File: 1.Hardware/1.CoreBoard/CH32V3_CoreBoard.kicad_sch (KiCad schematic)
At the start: 53 parts, among them J2 SH1.0_4P, J3 USB-Type-C, J4 BTB_02X18, J5 BTB_02X18, SW1 3x4, SW2 3x4, SW3 3x4, SW4 3x4, U2 RT9013-33GB, U3 BMI270, U5 IPS096, Y1 32.768KHz, Y2 8MHz

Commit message: coreboard
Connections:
- net ENC_2DIR: now also J5.32 (Pin_32); no longer J5.30 (Pin_30)
- net PB12: now also J5.27 (Pin_27); no longer J5.31 (Pin_31)
- net PB14: now also J5.36 (Pin_36); no longer J5.32 (Pin_32)
- net PD10: now also J5.30 (Pin_30); no longer J5.27 (Pin_27)
- net PD8: now also J5.34 (Pin_34); no longer J5.29 (Pin_29)
- net PE14: now also J5.31 (Pin_31); no longer J5.35 (Pin_35)
- net PE15: now also J5.29 (Pin_29); no longer J5.36 (Pin_36)
- net UART7_RX: now also J5.33 (Pin_33); no longer J5.34 (Pin_34)
- net UART7_TX: now also J5.35 (Pin_35); no longer J5.33 (Pin_33)

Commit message: CoreBoard finished
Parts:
- added C22: 100nF, ErBW_s:C_0402, symbol Device:C_Small
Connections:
- net +3.3V: now also C22.2
- net ADC_DIS: now also J4.4 (Pin_4); no longer J4.9 (Pin_9)
- net ADC_VBAT: now also J4.2 (Pin_2); no longer J4.10 (Pin_10)
- net AUX_SCL: now also J4.13 (Pin_13); no longer J4.1 (Pin_1)
- net AUX_SDA: now also J4.11 (Pin_11); no longer J4.2 (Pin_2)
- net BUZZER: now also J4.9 (Pin_9); no longer J4.3 (Pin_3)
- net ENCODER_B: now also U1.3 (PE4); no longer U1.2 (PE3)
- net ENC_1DIR: now also J4.27 (Pin_27); no longer J4.29 (Pin_29)
- net ENC_1LSB: now also J4.23 (Pin_23); no longer J4.27 (Pin_27)
- net GND: now also C22.1
- net KEY_CENTER: now also U1.2 (PE3); no longer U1.3 (PE4)
- net PA0: now also J4.6 (Pin_6); no longer J4.8 (Pin_8)
- net PA15: now also J4.29 (Pin_29); no longer J4.28 (Pin_28)
- net PA3: now also J4.8 (Pin_8); no longer J4.11 (Pin_11)
- net PA7: now also J4.10 (Pin_10); no longer J4.12 (Pin_12)
- net PB0: now also J4.16 (Pin_16); no longer J4.15 (Pin_15)
- net PB1: now also J4.18 (Pin_18); no longer J4.16 (Pin_16)
- net PC0: now also J4.7 (Pin_7); no longer J4.4 (Pin_4)
- net PC2: now also J4.3 (Pin_3); no longer J4.6 (Pin_6)
- net PC3: now also J4.1 (Pin_1); no longer J4.7 (Pin_7)
- net PC4: now also J4.12 (Pin_12); no longer J4.13 (Pin_13)
- net PD2: now also J4.25 (Pin_25); no longer J4.26 (Pin_26)
- net PD5: now also J4.21 (Pin_21); no longer J4.24 (Pin_24)
- net PD6: now also J4.19 (Pin_19); no longer J4.25 (Pin_25)
- net PE0: now also J4.17 (Pin_17); no longer J4.22 (Pin_22)
- net PE1: now also J4.15 (Pin_15); no longer J4.23 (Pin_23)
- net PE10: now also J4.26 (Pin_26); no longer J4.20 (Pin_20)
- net PE11: now also J4.28 (Pin_28); no longer J4.21 (Pin_21)
- net PE7: now also J4.20 (Pin_20); no longer J4.17 (Pin_17)
- net PE8: now also J4.22 (Pin_22); no longer J4.18 (Pin_18)
- net PE9: now also J4.24 (Pin_24); no longer J4.19 (Pin_19)
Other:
- moved on the sheet: C12, C13, C14, C15, C16, C17, C18, C19

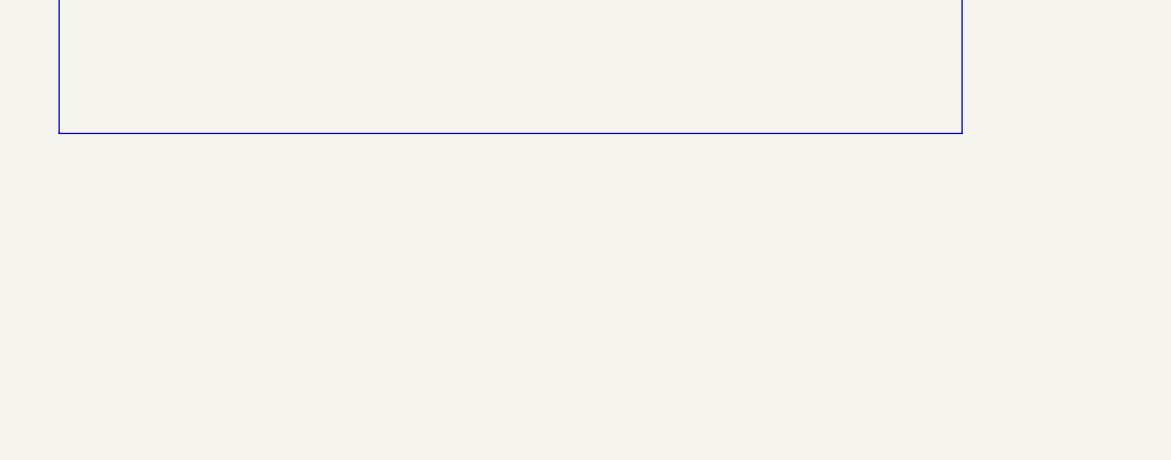
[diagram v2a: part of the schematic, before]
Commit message: MotherBoard power sch
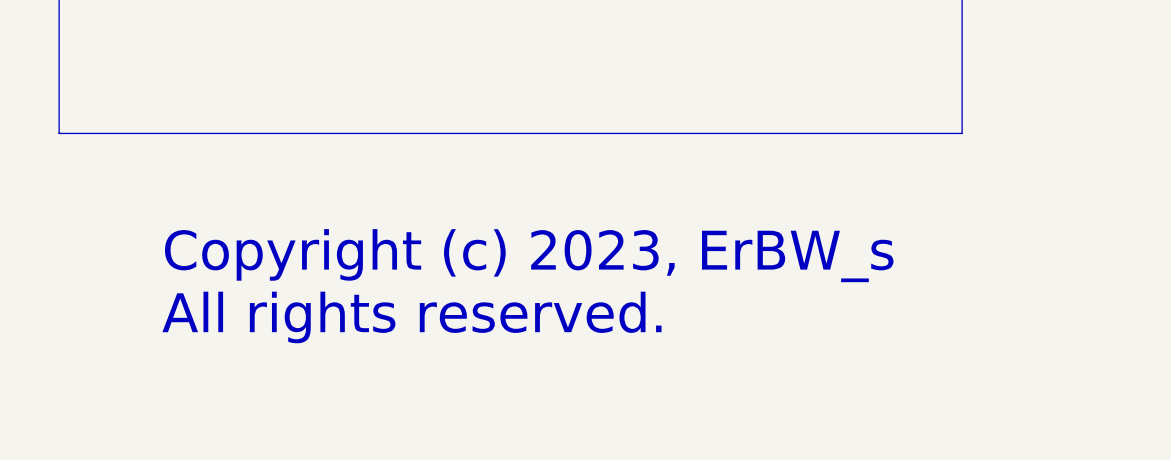
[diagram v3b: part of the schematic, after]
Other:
- note added: "Copyright (c) 2023, ErBW_s All rights reserved."
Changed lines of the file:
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@@
     (effects (font (size 3.048 3.048) (thickness 0.6096) bold) (justify left top))
+  )
+  (text "Copyright (c) 2023, ErBW_s\nAll rights reserved." (at 311.15 266.7 0)
+    (effects (font (size 4.318 4.318)) (justify left bottom))
   )
   (text "PWR" (at 19.05 22.86 0)

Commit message: MotherBoard finished
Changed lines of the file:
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@@
     (fill (type none))
   )
-  (text_box "ENCODER:D3&D1-TIM10 / D11&D9-TIM9\n\nBLDC:D12~D15-TIM4\n\nSERVO:A15-TIM2\n\nBUZZER:C13-TIM8"
-    (at 299.72 34.29 0) (size 100.33 39.37)
+  (text_box "ENCODER:\n	BLDC: D3&D1-TIM10\n	WHEEL: D11&D9-TIM9\n\nBLDC:PWM:D14 / DIR:D15 -TIM4\nWHEEL:PWM:D12 / DIR:D13 -TIM4\n\nSERVO:A15-TIM2\n\nBUZZER:C13-TIM8"
+    (at 299.72 25.4 0) (size 100.33 53.34)
     (stroke (width 0.127) (type dash_dot) (color 255 0 0 1))
     (fill (type color) (color 194 194 0 1))
